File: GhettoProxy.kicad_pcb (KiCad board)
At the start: 2 copper layers, 23 x 27 mm, 22 parts, among them IC1 ATMEGA328P-A, P1 OpenLRS, P2 Telemetrie, U1 MIC5205 3,3v, Y1 RESONATEUR

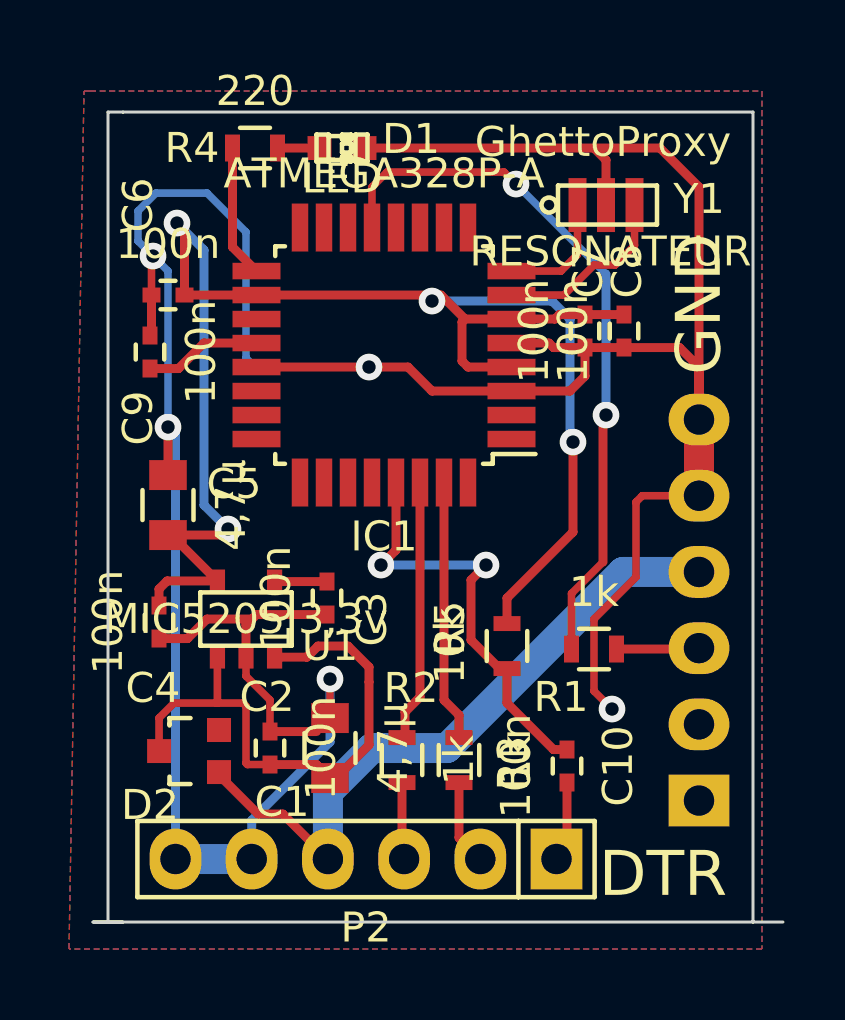
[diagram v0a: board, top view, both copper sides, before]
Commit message: 3,3V LDO entfernt (macht keinen Sinn und kostet nur Geld), Platine verkleinert
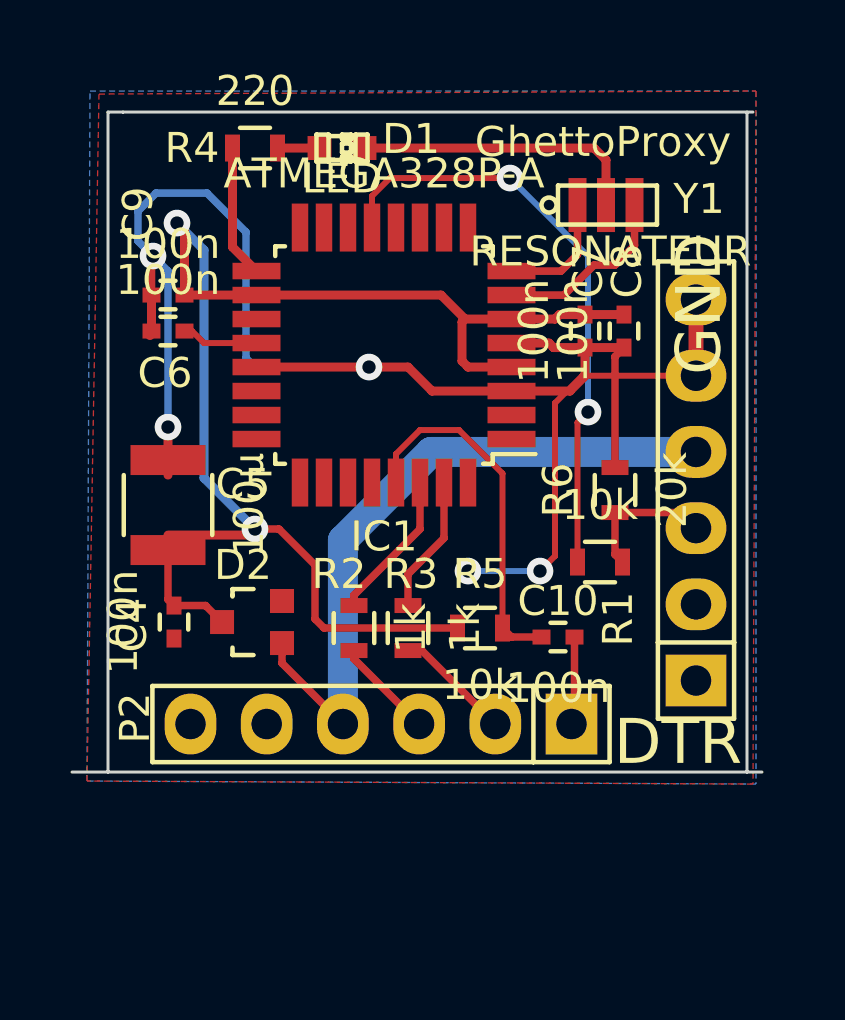
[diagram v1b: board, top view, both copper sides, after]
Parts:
- removed C1: 4,7µ, Capacitors_SMD:C_0805
- removed C2, C3: 100n, Capacitors_SMD:C_0402
- removed U1: MIC5205 3,3v, SMD_Packages:SOT-23-5
- added R6: 20k, Resistors_SMD:R_0603, F.Cu at (171.4, 111.6)
- C5: value 4,7µ -> 100µ; footprint Capacitors_SMD:C_0805 -> Capacitors_SMD:C_1210
- P1: moved to F.Cu
- R1: value 1k -> 10k
- moved D2 4.79 mm to (159.3, 116.0)
- moved R3 4.72 mm to (164.5, 116.2)
- moved R2 4.68 mm to (162.7, 116.2)
- moved P2 4.53 mm to (163.6, 119.4)
- moved C10 4.31 mm to (169.5, 116.5), turned to 0 degrees
- moved P1 4.00 mm to (174.1, 111.6)
- moved R1 2.91 mm to (170.9, 114.0)
- moved R5 1.08 mm to (166.9, 116.2), turned to 0 degrees
- moved C6 0.92 mm to (156.5, 106.3), turned to 180 degrees
- moved C4 0.50 mm to (156.7, 116.0)
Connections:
- C4 pad 1: +3.3V -> +5V
- C5 pad 1: +3.3V -> +5V
- C7 pad 1: +3.3V -> +5V
- C8 pad 1: +3.3V -> +5V
- C9 pad 1: +3.3V -> +5V
- D2 pad 1: +5V -> Net-(D2-Pad1)
- D2 pad 2: Net-(C1-Pad1) -> +5V
- IC1 pad 18: +3.3V -> +5V
- IC1 pad 4: +3.3V -> +5V
- IC1 pad 6: +3.3V -> +5V
- P1 pad 4: +5V -> Net-(D2-Pad1)
- P2 pad 4: +5V -> Net-(D2-Pad1)
- R5 pad 1: +3.3V -> +5V
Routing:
- net +3.3V: track 54.6 -> 0.00 mm, vias 4 -> 0
- net GND: track 116.6 -> 70.6 mm
- net +5V: track 25.6 -> 48.5 mm, vias 0 -> 2
- net Net-(D2-Pad1): track 0.00 -> 22.7 mm
- net Net-(C1-Pad1): track 21.8 -> 0.00 mm
- net Net-(IC1-Pad31): track 8.71 -> 4.60 mm
- net Net-(IC1-Pad13): track 23.7 -> 19.9 mm
- net Net-(IC1-Pad30): track 8.75 -> 5.01 mm
- net Net-(C10-Pad1): track 14.5 -> 12.0 mm, vias 2 -> 0
- net /LTMOUT: track 2.76 -> 4.67 mm
- net Net-(C3-Pad1): track 1.76 -> 0.00 mm
- net Net-(C6-Pad1): track 3.90 -> 2.57 mm
- net /TX: track 2.84 -> 3.92 mm
- net /RX: track 2.58 -> 3.49 mm
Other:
- board size 23 x 27 mm -> 23 x 22 mm
